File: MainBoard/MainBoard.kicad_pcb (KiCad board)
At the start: 2 copper layers, 111 parts, among them J1 DF40C-100DS-0.4V(51) _LFT, J2 DF40C-100DS-0.4V(51) _RFT (PN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, J3 HDMI_A, J4 Barrel_Jack, J7 USB_C_Receptacle, SW1 SW_Push, SW10 SW_Push, SW100 SW_Push, SW11 SW_Push, SW12 SW_Push, SW13 SW_Push, SW14 SW_Push, SW15 SW_Push, SW16 SW_Push, SW17 SW_Push, SW18 SW_Push, SW19 SW_Push, SW2 SW_Push, SW20 SW_Push, SW21 SW_Push, SW22 SW_Push, SW23 SW_Push, SW24 SW_Push, SW25 SW_Push, SW26 SW_Push, SW27 SW_Push, SW28 SW_Push, SW29 SW_Push, SW3 SW_Push, SW30 SW_Push, SW31 SW_Push, SW32 SW_Push, SW33 SW_Push, SW34 SW_Push, SW35 SW_Push, SW36 SW_Push, SW37 SW_Push, SW38 SW_Push, SW39 SW_Push, SW4 SW_Push, SW40 SW_Push, SW41 SW_Push, SW42 SW_Push, SW43 SW_Push, SW44 SW_Push, SW45 SW_Push, SW46 SW_Push, SW47 SW_Push, SW48 SW_Push, SW49 SW_Push, SW5 SW_Push, SW50 SW_Push, SW51 SW_Push, SW52 SW_Push, SW53 SW_Push, SW54 SW_Push, SW55 SW_Push, SW56 SW_Push, SW57 SW_Push, SW58 SW_Push, SW59 SW_Push, SW6 SW_Push, SW60 SW_Push, SW61 SW_Push, SW62 SW_Push, SW63 SW_Push, SW64 SW_Push, SW65 SW_Push, SW66 SW_Push, SW67 SW_Push, SW68 SW_Push, SW69 SW_Push, SW7 SW_Push, SW70 SW_Push, SW71 SW_Push, SW72 SW_Push, SW73 SW_Push, SW74 SW_Push, SW75 SW_Push, SW76 SW_Push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

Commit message: space out keyswitches for standard caps!
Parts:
- moved SW13 242.7 mm to (-15.0, 160.0)
- moved SW2 236.9 mm to (10.0, 160.0)
- moved SW5 231.4 mm to (35.0, 160.0)
- moved SW9 226.0 mm to (60.0, 160.0)
- moved SW1 217.0 mm to (-15.0, 140.0)
- moved SW14 215.3 mm to (95.0, 160.0)
- moved SW4 206.9 mm to (15.0, 140.0)
- moved SW20 203.5 mm to (135.0, 160.0)
- moved SW8 197.3 mm to (45.0, 140.0)
- moved SW27 195.7 mm to (170.0, 160.0)
- moved SW37 194.7 mm to (65.0, 140.0)
- moved SW3 194.6 mm to (-15.0, 120.0)
- moved SW35 192.6 mm to (195.0, 160.0)
- moved SW19 192.2 mm to (85.0, 140.0)
- moved SW43 191.4 mm to (215.0, 160.0)
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
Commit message: route keyboard
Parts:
- moved SW72 67.0 mm to (244.0, 138.0)
- moved SW1 66.5 mm to (49.0, 158.0)
- moved SW10 66.5 mm to (64.0, 98.0)
- moved SW100 66.5 mm to (304.0, 178.0)
- moved SW11 66.5 mm to (94.0, 118.0)
- moved SW13 66.5 mm to (49.0, 178.0)
- moved SW14 66.5 mm to (159.0, 178.0)
- moved SW15 66.5 mm to (64.0, 78.0)
- moved SW16 66.5 mm to (89.0, 98.0)
- moved SW17 66.5 mm to (114.0, 118.0)
- moved SW18 66.5 mm to (124.0, 138.0)
- moved SW19 66.5 mm to (149.0, 158.0)
- moved SW2 66.5 mm to (74.0, 178.0)
- moved SW20 66.5 mm to (199.0, 178.0)
- moved SW21 66.5 mm to (184.0, 78.1)
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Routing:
- net Net-(SW14-Pad1): track 0.00 -> 964.8 mm
- net Net-(SW13-Pad1): track 0.00 -> 893.0 mm
- net Net-(SW18-Pad1): track 0.00 -> 876.3 mm
- net Net-(SW12-Pad1): track 0.00 -> 848.7 mm
- net Net-(SW15-Pad1): track 0.00 -> 830.5 mm
- net Net-(SW19-Pad1): track 0.00 -> 780.6 mm
- net Net-(SW1-Pad1): track 0.00 -> 664.5 mm, vias 0 -> 2
- net Net-(SW17-Pad1): track 0.00 -> 630.5 mm
- net Net-(SW16-Pad1): track 0.00 -> 619.3 mm
- net Net-(SW10-Pad1): track 0.00 -> 573.6 mm
- net Net-(SW41-Pad2): track 0.00 -> 542.1 mm
- net Net-(SW21-Pad2): track 0.00 -> 525.9 mm
- net Net-(SW100-Pad2): track 0.00 -> 518.7 mm
- net Net-(SW51-Pad2): track 0.00 -> 494.6 mm
- net Net-(SW81-Pad2): track 0.00 -> 468.5 mm
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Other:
- board outline added: 340 x 200 mm
- copper layers 2 -> 6

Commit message: move power dilevery to a hierarchy sheet and wire HDMI1
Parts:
- moved J1 306.7 mm to (75.4, 239.0), turned to 180 degrees
- moved J2 267.2 mm to (75.4, 204.9), turned to 180 degrees
- moved U1 101.0 mm to (161.0, -53.0), turned to 270 degrees
- moved SW1 14.2 mm to (40.0, 147.0)
- moved SW10 14.2 mm to (55.0, 87.0)
- moved SW100 14.2 mm to (295.0, 167.0)
- moved SW11 14.2 mm to (85.0, 107.0)
- moved SW12 14.2 mm to (115.0, 67.0)
- moved SW13 14.2 mm to (40.0, 167.0)
- moved SW14 14.2 mm to (150.0, 167.0)
- moved SW15 14.2 mm to (55.0, 67.0)
- moved SW16 14.2 mm to (80.0, 87.0)
- moved SW17 14.2 mm to (105.0, 107.0)
- moved SW18 14.2 mm to (115.0, 127.0)
- moved SW19 14.2 mm to (140.0, 147.0)
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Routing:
- net Net-(SW31-Pad2): track 346.6 -> 380.4 mm
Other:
- board size 340 x 200 mm -> 340 x 230 mm

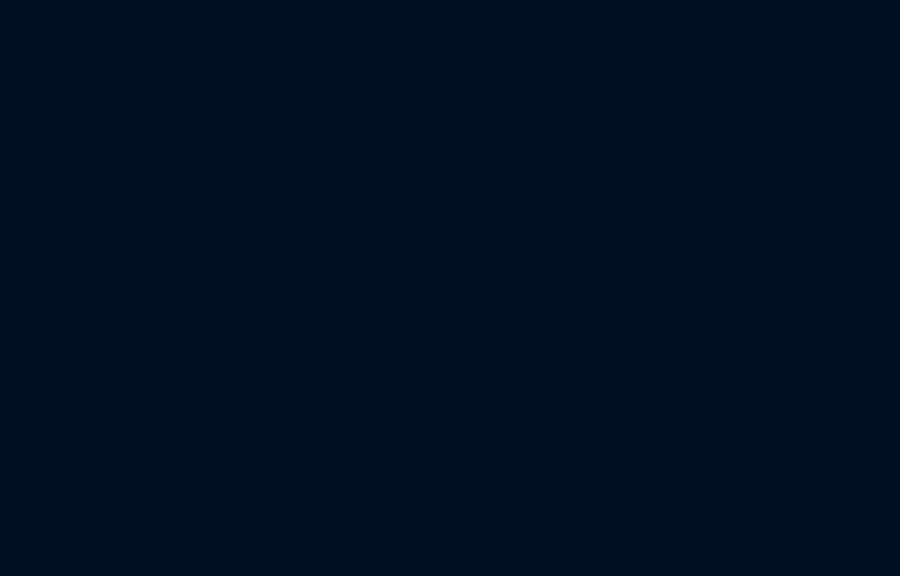
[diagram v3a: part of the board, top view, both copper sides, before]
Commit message: Add usb 3 chip in hierarchy sheet and wire ports
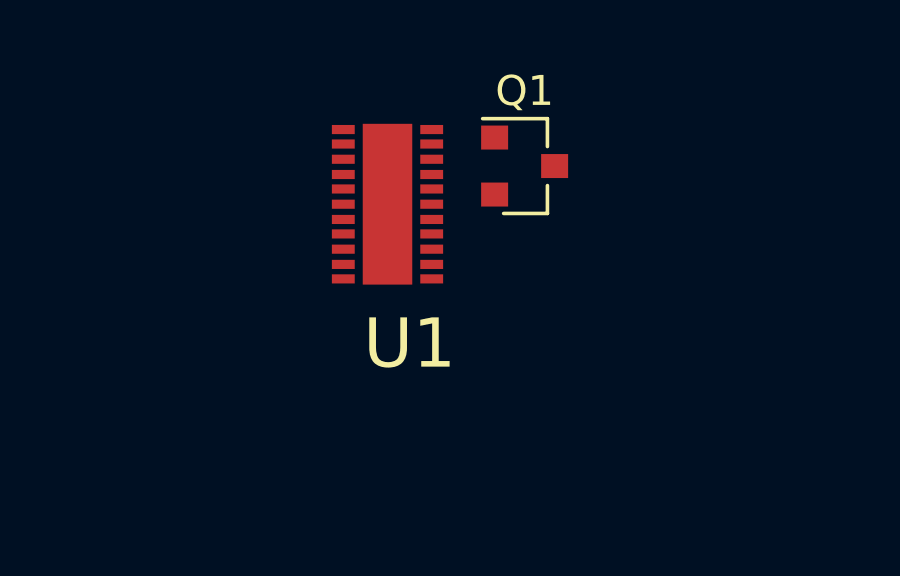
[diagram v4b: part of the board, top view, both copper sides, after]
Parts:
- added Q1: AO3401A, Package_TO_SOT_SMD:SOT-23, F.Cu at (185.5, -83.3)
- added U1: LTC4090EDJCPBF, Libs:DFN600X300X80-23N, F.Cu at (180.9, -82.0)
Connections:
- J3 pad 1: Net-(J3-Pad1) -> Net-(J2-Pad46)
- J3 pad 10: Net-(J3-Pad10) -> Net-(J2-Pad64)
- J3 pad 11: Net-(J3-Pad11) -> GND
- J3 pad 12: Net-(J3-Pad12) -> Net-(J2-Pad66)
- J3 pad 13: Net-(J3-Pad13) -> Net-(J2-Pad49)
- J3 pad 15: Net-(J3-Pad15) -> Net-(J2-Pad47)
- J3 pad 16: Net-(J3-Pad16) -> Net-(J2-Pad45)
- J3 pad 17: Net-(J3-Pad17) -> GND
- J3 pad 18: Net-(J3-Pad18) -> +5V
- J3 pad 19: Net-(J3-Pad19) -> Net-(J2-Pad43)
- J3 pad 2: Net-(J3-Pad2) -> GND
- J3 pad 3: Net-(J3-Pad3) -> Net-(J2-Pad48)
- J3 pad 4: Net-(J3-Pad4) -> Net-(J2-Pad52)
- J3 pad 5: Net-(J3-Pad5) -> GND
- J3 pad 6: Net-(J3-Pad6) -> Net-(J2-Pad54)
- J3 pad 7: Net-(J3-Pad7) -> Net-(J2-Pad58)
- J3 pad 8: Net-(J3-Pad8) -> GND
- J3 pad 9: Net-(J3-Pad9) -> Net-(J2-Pad60)
- J3 pad SH: Net-(J3-PadSH) -> GND
- J4 pad 2: Net-(J4-Pad2) -> /Power_Delivery/HV_IN
- J7 pad A4: Net-(J7-PadA4) -> /Power_Delivery/5v_IN
- J7 pad A5: Net-(J7-PadA5) -> Net-(J1-Pad96)
- J7 pad A9: Net-(J7-PadA4) -> /Power_Delivery/5v_IN
- J7 pad B4: Net-(J7-PadA4) -> /Power_Delivery/5v_IN
- J7 pad B5: Net-(J7-PadB5) -> Net-(J1-Pad94)
- J7 pad B9: Net-(J7-PadA4) -> /Power_Delivery/5v_IN

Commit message: mostly replace keyboard
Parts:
- removed BT2, BT3, BT4: _, Connector_JST:JST_PH_S2B-PH-SM4-TB_1x02-1MP_P2.00mm_Horizontal
- removed the U1 at (180.9, -82.0)
- removed the U1 at (161.0, -53.0)
- added C1: 270pF, LED_SMD:LED_0805_2012Metric_Castellated, F.Cu at (556.1, -145.0)
- added C2: 0.1uF, LED_SMD:LED_0805_2012Metric_Castellated, F.Cu at (565.8, -145.0)
- added C3: 4.7uF, LED_SMD:LED_0805_2012Metric_Castellated, F.Cu at (570.8, -154.1)
- added C4: 1uF, LED_SMD:LED_0805_2012Metric_Castellated, F.Cu at (561.0, -145.0)
- added C5: 0.47uF, LED_SMD:LED_0805_2012Metric_Castellated, F.Cu at (570.8, -157.0)
- added C6: 22uF, LED_SMD:LED_0805_2012Metric_Castellated, F.Cu at (556.1, -149.9)
- added D1: D_Schottky, LED_THT:LED_D1.8mm_W1.8mm_H2.4mm_Horizontal_O6.35mm_Z8.2mm, F.Cu at (564.1, -156.7)
- added J10: USB3_A, Connector_USB:USB3_A_Plug_Wuerth_692112030100_Horizontal, F.Cu at (479.2, -135.5)
- added J11: USB3_A (FAST), Connector_USB:USB3_A_Plug_Wuerth_692112030100_Horizontal, F.Cu at (479.2, -150.8)
- added J5: USB3_A, Connector_USB:USB3_A_Plug_Wuerth_692112030100_Horizontal, F.Cu at (525.6, -150.8)
- added J6: USB3_A, Connector_USB:USB3_A_Plug_Wuerth_692112030100_Horizontal, F.Cu at (502.4, -135.5)
- added J9: USB3_A, Connector_USB:USB3_A_Plug_Wuerth_692112030100_Horizontal, F.Cu at (502.4, -150.8)
- added U1: LTC4090EDJCPBF, Libs:DFN600X300X80-23N, F.Cu at (551.3, -147.8)
- added U3: CD74HC4067M, Package_SO:SOIC-24W_7.5x15.4mm_P1.27mm, F.Cu at (513.1, -111.5)
- added U4: TUSB8041, Package_DFN_QFN:QFN-64-1EP_9x9mm_P0.5mm_EP6x6mm_ThermalVias, F.Cu at (527.6, -137.5)
- BT1: value Battery Cell -> Battery_Cell; footprint Connector_JST:JST_PH_S2B-PH-SM4-TB_1x02-1MP_P2.00mm_Horizontal -> Connector_PinSocket_2.54mm:PinSocket_1x02_P2.54mm_Horizontal
- SW1, SW10, SW100, SW11, SW12, SW13, SW14, SW15, SW16, SW17, SW18, SW19, SW2, SW20, SW21, SW22, SW23, SW24, SW25, SW26, SW27, SW28, SW29, SW3, SW30, SW31, SW32, SW33, SW34, SW35, SW36, SW37, SW38, SW39, SW4, SW40, SW41, SW42, SW43, SW44, SW45, SW46, SW47, SW48, SW49, SW5, SW50, SW51, SW52, SW53, SW54, SW55, SW56, SW57, SW58, SW59, SW6, SW60, SW61, SW62, SW63, SW64, SW65, SW66, SW67, SW68, SW69, SW7, SW70, SW71, SW72, SW73, SW74, SW75, SW76, SW77, SW78, SW79, SW8, SW80, SW81, SW82, SW83, SW84, SW85, SW86, SW87, SW88, SW89, SW9, SW90, SW91, SW92, SW93, SW94, SW95, SW96, SW97, SW98, SW99: value SW_Push -> SW_MEC_5G; footprint Libs:SW_PG1350_reversible_rotatable -> Libs:Kailh_socket_PG1350
- moved J1 594.5 mm to (492.5, -184.6), turned to 0 degrees
- moved J2 566.9 mm to (492.5, -179.0), turned to 0 degrees
- moved U2 467.9 mm to (480.1, -115.6)
- moved Q1 390.9 mm to (570.6, -150.3)
- moved SW5 378.7 mm to (243.2, -179.3)
- moved SW94 345.7 mm to (50.0, 260.0)
- moved SW4 341.5 mm to (170.6, -179.3)
- moved SW11 336.3 mm to (261.4, -179.3)
- moved SW9 331.4 mm to (225.1, -145.6)
- moved BT1 322.6 mm to (560.1, -156.2)
- moved SW2 320.6 mm to (188.8, -128.8)
- moved SW3 319.7 mm to (206.9, -145.6)
- moved SW28 319.0 mm to (370.0, 180.0)
- moved SW95 314.5 mm to (75.0, 260.0)
- moved SW10 312.5 mm to (243.2, -162.5)
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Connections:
- net Net-(J2-Pad10) renamed PCIe_CLK_P
- net Net-(J2-Pad12) renamed PCIe_CLK_N
- net Net-(J2-Pad16) renamed PCIe_RX_P
- net Net-(J2-Pad18) renamed PCIe_RX_N
- net Net-(J2-Pad2) renamed PCIe_CLK_nREQ
- net Net-(J2-Pad22) renamed PCIe_TX_P
- net Net-(J2-Pad24) renamed PCIe_TX_N
- net Net-(J2-Pad9) renamed PCIe_nRST
- J7 pad A10: Net-(J7-PadA10) -> USBCRXN
- J7 pad A11: Net-(J7-PadA11) -> USBCRXP
- J7 pad A2: Net-(J7-PadA2) -> USBCTXP
- J7 pad A3: Net-(J7-PadA3) -> USBCTXN
- J7 pad A6: Net-(J7-PadA6) -> USBCP
- J7 pad A7: Net-(J7-PadA7) -> USBCM
- J7 pad B10: Net-(J7-PadB10) -> USBCRXN
- J7 pad B11: Net-(J7-PadB11) -> USBCRXP
- J7 pad B2: Net-(J7-PadB2) -> USBCTXP
- J7 pad B3: Net-(J7-PadB3) -> USBCTXN
- J7 pad B6: Net-(J7-PadB6) -> USBCP
- J7 pad B7: Net-(J7-PadB7) -> USBCM
- SW1 pad 2: Net-(SW1-Pad2) -> Net-(SW1-Pad1)
- SW10 pad 2: Net-(SW1-Pad2) -> Net-(SW10-Pad1)
- SW100 pad 1: Net-(SW10-Pad1) -> Net-(SW100-Pad1)
- SW100 pad 2: Net-(SW100-Pad2) -> Net-(SW100-Pad1)
- SW11 pad 1: Net-(SW1-Pad1) -> Net-(SW11-Pad1)
- SW11 pad 2: Net-(SW11-Pad2) -> Net-(SW11-Pad1)
- SW12 pad 2: Net-(SW11-Pad2) -> Net-(SW12-Pad1)
- SW13 pad 1: Net-(SW13-Pad1) -> Net-(SW1-Pad1)
- SW13 pad 2: Net-(SW11-Pad2) -> Net-(SW1-Pad1)
- SW14 pad 2: Net-(SW11-Pad2) -> Net-(SW14-Pad1)
- SW15 pad 2: Net-(SW11-Pad2) -> Net-(SW15-Pad1)
- SW16 pad 2: Net-(SW11-Pad2) -> Net-(SW16-Pad1)
- SW17 pad 2: Net-(SW11-Pad2) -> Net-(SW17-Pad1)
- SW18 pad 2: Net-(SW11-Pad2) -> Net-(SW18-Pad1)
- SW19 pad 1: Net-(SW19-Pad1) -> Net-(SW100-Pad1)
- SW19 pad 2: Net-(SW11-Pad2) -> Net-(SW100-Pad1)
- SW2 pad 1: Net-(SW12-Pad1) -> Net-(SW14-Pad1)
- SW2 pad 2: Net-(SW1-Pad2) -> Net-(SW14-Pad1)
- SW20 pad 1: Net-(SW10-Pad1) -> Net-(SW20-Pad1)
- SW20 pad 2: Net-(SW11-Pad2) -> Net-(SW20-Pad1)
- SW21 pad 1: Net-(SW1-Pad1) -> Net-(SW21-Pad1)
- SW21 pad 2: Net-(SW21-Pad2) -> Net-(SW21-Pad1)
- SW22 pad 1: Net-(SW12-Pad1) -> Net-(SW22-Pad1)
- SW22 pad 2: Net-(SW21-Pad2) -> Net-(SW22-Pad1)
- SW23 pad 1: Net-(SW13-Pad1) -> Net-(SW23-Pad1)
- SW23 pad 2: Net-(SW21-Pad2) -> Net-(SW23-Pad1)
- SW24 pad 1: Net-(SW14-Pad1) -> Net-(SW10-Pad1)
- SW24 pad 2: Net-(SW21-Pad2) -> Net-(SW10-Pad1)
- SW25 pad 1: Net-(SW15-Pad1) -> Net-(SW25-Pad1)
- SW25 pad 2: Net-(SW21-Pad2) -> Net-(SW25-Pad1)
- SW26 pad 1: Net-(SW16-Pad1) -> Net-(SW11-Pad1)
- SW26 pad 2: Net-(SW21-Pad2) -> Net-(SW11-Pad1)
- SW27 pad 1: Net-(SW17-Pad1) -> Net-(SW27-Pad1)
- SW27 pad 2: Net-(SW21-Pad2) -> Net-(SW27-Pad1)
- SW28 pad 1: Net-(SW18-Pad1) -> Net-(SW27-Pad1)
- SW28 pad 2: Net-(SW21-Pad2) -> Net-(SW27-Pad1)
- SW29 pad 1: Net-(SW19-Pad1) -> Net-(SW12-Pad1)
- SW29 pad 2: Net-(SW21-Pad2) -> Net-(SW12-Pad1)
- SW3 pad 1: Net-(SW13-Pad1) -> Net-(SW15-Pad1)
- SW3 pad 2: Net-(SW1-Pad2) -> Net-(SW15-Pad1)
- SW30 pad 1: Net-(SW10-Pad1) -> Net-(SW1-Pad1)
- SW30 pad 2: Net-(SW21-Pad2) -> Net-(SW1-Pad1)
- SW31 pad 1: Net-(SW1-Pad1) -> Net-(SW15-Pad1)
- SW31 pad 2: Net-(SW31-Pad2) -> Net-(SW15-Pad1)
- SW32 pad 1: Net-(SW12-Pad1) -> Net-(SW16-Pad1)
- SW32 pad 2: Net-(SW31-Pad2) -> Net-(SW16-Pad1)
- SW33 pad 1: Net-(SW13-Pad1) -> Net-(SW17-Pad1)
- SW33 pad 2: Net-(SW31-Pad2) -> Net-(SW17-Pad1)
- SW34 pad 1: Net-(SW14-Pad1) -> Net-(SW18-Pad1)
- SW34 pad 2: Net-(SW31-Pad2) -> Net-(SW18-Pad1)
- SW35 pad 1: Net-(SW15-Pad1) -> Net-(SW100-Pad1)
- SW35 pad 2: Net-(SW31-Pad2) -> Net-(SW100-Pad1)
- SW36 pad 1: Net-(SW16-Pad1) -> Net-(SW20-Pad1)
- SW36 pad 2: Net-(SW31-Pad2) -> Net-(SW20-Pad1)
- SW37 pad 1: Net-(SW17-Pad1) -> Net-(SW21-Pad1)
- SW37 pad 2: Net-(SW31-Pad2) -> Net-(SW21-Pad1)
- SW38 pad 1: Net-(SW18-Pad1) -> Net-(SW22-Pad1)
- SW38 pad 2: Net-(SW31-Pad2) -> Net-(SW22-Pad1)
- SW39 pad 1: Net-(SW19-Pad1) -> Net-(SW23-Pad1)
- SW39 pad 2: Net-(SW31-Pad2) -> Net-(SW23-Pad1)
- SW4 pad 1: Net-(SW14-Pad1) -> Net-(SW16-Pad1)
- SW4 pad 2: Net-(SW1-Pad2) -> Net-(SW16-Pad1)
- SW40 pad 2: Net-(SW31-Pad2) -> Net-(SW10-Pad1)
- SW41 pad 1: Net-(SW1-Pad1) -> Net-(SW25-Pad1)
- SW41 pad 2: Net-(SW41-Pad2) -> Net-(SW25-Pad1)
- SW42 pad 1: Net-(SW12-Pad1) -> Net-(SW11-Pad1)
- SW42 pad 2: Net-(SW41-Pad2) -> Net-(SW11-Pad1)
- SW43 pad 1: Net-(SW13-Pad1) -> Net-(SW12-Pad1)
- SW43 pad 2: Net-(SW41-Pad2) -> Net-(SW12-Pad1)
- SW44 pad 2: Net-(SW41-Pad2) -> Net-(SW14-Pad1)
- SW45 pad 2: Net-(SW41-Pad2) -> Net-(SW15-Pad1)
- SW46 pad 2: Net-(SW41-Pad2) -> Net-(SW16-Pad1)
- SW47 pad 2: Net-(SW41-Pad2) -> Net-(SW17-Pad1)
- SW48 pad 2: Net-(SW41-Pad2) -> Net-(SW18-Pad1)
- SW49 pad 1: Net-(SW19-Pad1) -> Net-(SW100-Pad1)
- SW49 pad 2: Net-(SW41-Pad2) -> Net-(SW100-Pad1)
- SW5 pad 1: Net-(SW15-Pad1) -> Net-(SW17-Pad1)
- SW5 pad 2: Net-(SW1-Pad2) -> Net-(SW17-Pad1)
- SW50 pad 1: Net-(SW10-Pad1) -> Net-(SW20-Pad1)
- SW50 pad 2: Net-(SW41-Pad2) -> Net-(SW20-Pad1)
- SW51 pad 1: Net-(SW1-Pad1) -> Net-(SW21-Pad1)
- SW51 pad 2: Net-(SW51-Pad2) -> Net-(SW21-Pad1)
- SW52 pad 1: Net-(SW12-Pad1) -> Net-(SW22-Pad1)
- SW52 pad 2: Net-(SW51-Pad2) -> Net-(SW22-Pad1)
- SW53 pad 1: Net-(SW13-Pad1) -> Net-(SW23-Pad1)
- SW53 pad 2: Net-(SW51-Pad2) -> Net-(SW23-Pad1)
- SW54 pad 1: Net-(SW14-Pad1) -> Net-(SW10-Pad1)
- SW54 pad 2: Net-(SW51-Pad2) -> Net-(SW10-Pad1)
- SW55 pad 1: Net-(SW15-Pad1) -> Net-(SW25-Pad1)
- SW55 pad 2: Net-(SW51-Pad2) -> Net-(SW25-Pad1)
- SW56 pad 1: Net-(SW16-Pad1) -> Net-(SW11-Pad1)
- SW56 pad 2: Net-(SW51-Pad2) -> Net-(SW11-Pad1)
- SW57 pad 1: Net-(SW17-Pad1) -> Net-(SW27-Pad1)
- SW57 pad 2: Net-(SW51-Pad2) -> Net-(SW27-Pad1)
- SW58 pad 1: Net-(SW18-Pad1) -> Net-(SW12-Pad1)
- SW58 pad 2: Net-(SW51-Pad2) -> Net-(SW12-Pad1)
- SW59 pad 1: Net-(SW19-Pad1) -> Net-(SW1-Pad1)
- SW59 pad 2: Net-(SW51-Pad2) -> Net-(SW1-Pad1)
- SW6 pad 1: Net-(SW16-Pad1) -> Net-(SW100-Pad1)
- SW6 pad 2: Net-(SW1-Pad2) -> Net-(SW100-Pad1)
- SW60 pad 1: Net-(SW10-Pad1) -> Net-(SW14-Pad1)
- SW60 pad 2: Net-(SW51-Pad2) -> Net-(SW14-Pad1)
- SW61 pad 1: Net-(SW1-Pad1) -> Net-(SW15-Pad1)
- SW61 pad 2: Net-(SW61-Pad2) -> Net-(SW15-Pad1)
- SW62 pad 1: Net-(SW12-Pad1) -> Net-(SW16-Pad1)
- SW62 pad 2: Net-(SW61-Pad2) -> Net-(SW16-Pad1)
- SW63 pad 1: Net-(SW13-Pad1) -> Net-(SW17-Pad1)
- SW63 pad 2: Net-(SW61-Pad2) -> Net-(SW17-Pad1)
- SW64 pad 1: Net-(SW14-Pad1) -> Net-(SW18-Pad1)
- SW64 pad 2: Net-(SW61-Pad2) -> Net-(SW18-Pad1)
- SW65 pad 1: Net-(SW15-Pad1) -> Net-(SW100-Pad1)
- SW65 pad 2: Net-(SW61-Pad2) -> Net-(SW100-Pad1)
- SW66 pad 1: Net-(SW16-Pad1) -> Net-(SW20-Pad1)
- SW66 pad 2: Net-(SW61-Pad2) -> Net-(SW20-Pad1)
- SW67 pad 1: Net-(SW17-Pad1) -> Net-(SW21-Pad1)
- SW67 pad 2: Net-(SW61-Pad2) -> Net-(SW21-Pad1)
- SW68 pad 1: Net-(SW18-Pad1) -> Net-(SW22-Pad1)
- SW68 pad 2: Net-(SW61-Pad2) -> Net-(SW22-Pad1)
- SW69 pad 1: Net-(SW19-Pad1) -> Net-(SW23-Pad1)
- SW69 pad 2: Net-(SW61-Pad2) -> Net-(SW23-Pad1)
- SW7 pad 1: Net-(SW17-Pad1) -> Net-(SW20-Pad1)
- SW7 pad 2: Net-(SW1-Pad2) -> Net-(SW20-Pad1)
- SW70 pad 2: Net-(SW61-Pad2) -> Net-(SW10-Pad1)
- SW71 pad 1: Net-(SW1-Pad1) -> Net-(SW11-Pad1)
- SW71 pad 2: Net-(SW71-Pad2) -> Net-(SW11-Pad1)
- SW72 pad 1: Net-(SW12-Pad1) -> Net-(SW27-Pad1)
- SW72 pad 2: Net-(SW71-Pad2) -> Net-(SW27-Pad1)
- SW73 pad 1: Net-(SW13-Pad1) -> Net-(SW12-Pad1)
- SW73 pad 2: Net-(SW71-Pad2) -> Net-(SW12-Pad1)
- SW74 pad 1: Net-(SW14-Pad1) -> Net-(SW1-Pad1)
- SW74 pad 2: Net-(SW71-Pad2) -> Net-(SW1-Pad1)
- SW75 pad 1: Net-(SW15-Pad1) -> Net-(SW14-Pad1)
- SW75 pad 2: Net-(SW71-Pad2) -> Net-(SW14-Pad1)
- SW76 pad 1: Net-(SW16-Pad1) -> Net-(SW15-Pad1)
- SW76 pad 2: Net-(SW71-Pad2) -> Net-(SW15-Pad1)
- SW77 pad 1: Net-(SW17-Pad1) -> Net-(SW16-Pad1)
- SW77 pad 2: Net-(SW71-Pad2) -> Net-(SW16-Pad1)
- SW78 pad 1: Net-(SW18-Pad1) -> Net-(SW17-Pad1)
- SW78 pad 2: Net-(SW71-Pad2) -> Net-(SW17-Pad1)
- SW79 pad 1: Net-(SW19-Pad1) -> Net-(SW18-Pad1)
- SW79 pad 2: Net-(SW71-Pad2) -> Net-(SW18-Pad1)
- SW8 pad 1: Net-(SW18-Pad1) -> Net-(SW21-Pad1)
- SW8 pad 2: Net-(SW1-Pad2) -> Net-(SW21-Pad1)
- SW80 pad 1: Net-(SW10-Pad1) -> Net-(SW100-Pad1)
- SW80 pad 2: Net-(SW71-Pad2) -> Net-(SW100-Pad1)
- SW81 pad 1: Net-(SW1-Pad1) -> Net-(SW20-Pad1)
- SW81 pad 2: Net-(SW81-Pad2) -> Net-(SW20-Pad1)
- SW82 pad 1: Net-(SW12-Pad1) -> Net-(SW21-Pad1)
- SW82 pad 2: Net-(SW81-Pad2) -> Net-(SW21-Pad1)
- SW83 pad 1: Net-(SW13-Pad1) -> Net-(SW22-Pad1)
- SW83 pad 2: Net-(SW81-Pad2) -> Net-(SW22-Pad1)
- SW84 pad 1: Net-(SW14-Pad1) -> Net-(SW23-Pad1)
- SW84 pad 2: Net-(SW81-Pad2) -> Net-(SW23-Pad1)
- SW85 pad 1: Net-(SW15-Pad1) -> Net-(SW11-Pad1)
- SW85 pad 2: Net-(SW81-Pad2) -> Net-(SW11-Pad1)
- SW86 pad 1: Net-(SW16-Pad1) -> Net-(SW27-Pad1)
- SW86 pad 2: Net-(SW81-Pad2) -> Net-(SW27-Pad1)
- SW87 pad 1: Net-(SW17-Pad1) -> Net-(SW10-Pad1)
- SW87 pad 2: Net-(SW81-Pad2) -> Net-(SW10-Pad1)
- SW88 pad 1: Net-(SW18-Pad1) -> Net-(SW20-Pad1)
- SW88 pad 2: Net-(SW81-Pad2) -> Net-(SW20-Pad1)
- SW89 pad 1: Net-(SW19-Pad1) -> Net-(SW22-Pad1)
- SW89 pad 2: Net-(SW81-Pad2) -> Net-(SW22-Pad1)
- SW9 pad 1: Net-(SW19-Pad1) -> Net-(SW23-Pad1)
- SW9 pad 2: Net-(SW1-Pad2) -> Net-(SW23-Pad1)
- SW90 pad 1: Net-(SW10-Pad1) -> Net-(SW23-Pad1)
- SW90 pad 2: Net-(SW81-Pad2) -> Net-(SW23-Pad1)
- SW91 pad 1: Net-(SW1-Pad1) -> Net-(SW10-Pad1)
- SW91 pad 2: Net-(SW100-Pad2) -> Net-(SW10-Pad1)
- SW92 pad 1: Net-(SW12-Pad1) -> Net-(SW11-Pad1)
- SW92 pad 2: Net-(SW100-Pad2) -> Net-(SW11-Pad1)
- SW93 pad 1: Net-(SW13-Pad1) -> Net-(SW27-Pad1)
- SW93 pad 2: Net-(SW100-Pad2) -> Net-(SW27-Pad1)
- SW94 pad 1: Net-(SW14-Pad1) -> Net-(SW12-Pad1)
- SW94 pad 2: Net-(SW100-Pad2) -> Net-(SW12-Pad1)
- SW95 pad 1: Net-(SW15-Pad1) -> Net-(SW1-Pad1)
- SW95 pad 2: Net-(SW100-Pad2) -> Net-(SW1-Pad1)
- SW96 pad 1: Net-(SW16-Pad1) -> Net-(SW14-Pad1)
- SW96 pad 2: Net-(SW100-Pad2) -> Net-(SW14-Pad1)
- SW97 pad 1: Net-(SW17-Pad1) -> Net-(SW15-Pad1)
- SW97 pad 2: Net-(SW100-Pad2) -> Net-(SW15-Pad1)
- SW98 pad 1: Net-(SW18-Pad1) -> Net-(SW16-Pad1)
- SW98 pad 2: Net-(SW100-Pad2) -> Net-(SW16-Pad1)
- SW99 pad 1: Net-(SW19-Pad1) -> Net-(SW17-Pad1)
- SW99 pad 2: Net-(SW100-Pad2) -> Net-(SW17-Pad1)
- U2 pad 1: Net-(SW51-Pad2) -> Net-(U2-Pad1)
- U2 pad 12: Net-(SW11-Pad2) -> Net-(SW28-Pad3)
- U2 pad 19: Net-(SW100-Pad2) -> Net-(U2-Pad19)
- U2 pad 20: Net-(SW19-Pad1) -> Net-(U2-Pad20)
- U2 pad 21: Net-(SW18-Pad1) -> Net-(U2-Pad21)
- U2 pad 25: Net-(SW81-Pad2) -> Net-(U2-Pad25)
- U2 pad 26: Net-(SW1-Pad2) -> Net-(SW43-Pad3)
- U2 pad 27: Net-(SW61-Pad2) -> Net-(U2-Pad27)
- U2 pad 28: Net-(SW41-Pad2) -> Net-(U2-Pad28)
- U2 pad 29: Net-(SW31-Pad2) -> Net-(SW1-Pad3)
- U2 pad 30: Net-(SW21-Pad2) -> Net-(SW12-Pad3)
- U2 pad 31: Net-(SW71-Pad2) -> Net-(U2-Pad31)
- U2 pad 32: Net-(SW1-Pad1) -> Net-(SW58-Pad3)
- U2 pad 36: Net-(SW12-Pad1) -> Net-(SW73-Pad3)
- U2 pad 37: Net-(SW13-Pad1) -> Net-(SW100-Pad3)
- U2 pad 38: Net-(SW14-Pad1) -> Net-(U2-Pad38)
- U2 pad 39: Net-(SW15-Pad1) -> Net-(U2-Pad39)
- U2 pad 40: Net-(SW16-Pad1) -> Net-(U2-Pad40)
- U2 pad 41: Net-(SW17-Pad1) -> Net-(U2-Pad41)
- U2 pad 9: Net-(SW10-Pad1) -> Net-(U2-Pad9)
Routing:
- net Net-(SW14-Pad1): track 964.8 -> 0.00 mm
- net Net-(SW13-Pad1): track 893.0 -> 0.00 mm
- net Net-(SW18-Pad1): track 876.3 -> 0.00 mm
- net Net-(SW12-Pad1): track 848.7 -> 0.00 mm
- net Net-(SW15-Pad1): track 830.5 -> 0.00 mm
- net Net-(SW19-Pad1): track 780.6 -> 0.00 mm
- net Net-(SW1-Pad1): track 664.5 -> 0.00 mm, vias 2 -> 0
- net Net-(SW17-Pad1): track 630.5 -> 0.00 mm
- net Net-(SW16-Pad1): track 619.3 -> 0.00 mm
- net Net-(SW10-Pad1): track 573.6 -> 0.00 mm
- net Net-(SW41-Pad2): track 542.1 -> 0.00 mm
- net Net-(SW21-Pad2): track 525.9 -> 0.00 mm
- net Net-(SW100-Pad2): track 518.7 -> 0.00 mm
- net Net-(SW51-Pad2): track 494.6 -> 0.00 mm
- net Net-(SW81-Pad2): track 468.5 -> 0.00 mm
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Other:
- board outline removed

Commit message: mostly replace keyboard
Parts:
- moved U3 373.7 mm to (205.0, 100.0), turned to 180 degrees
- moved U2 301.5 mm to (255.0, 85.0), turned to 270 degrees

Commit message: finish keyboard, do some USB/PCIe routing
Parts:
- added U5: UPD720201K8-711-BAC-A, Libs:UPD720201K8-711-BAC-A, F.Cu at (219.8, 294.3)
- added U6: MX25L5121EMC-20G, Libs:MX25L5121EMC-20G, F.Cu at (236.0, 295.0)
- U2, U3: moved to B.Cu
- moved J5 657.4 mm to (51.0, 304.0), turned to 180 degrees
- moved J9 625.4 mm to (51.0, 282.0), turned to 180 degrees
- moved J2 556.0 mm to (226.0, 309.0)
- moved J10 555.8 mm to (139.5, 304.5), turned to 270 degrees
- moved U4 544.0 mm to (181.1, 281.9), turned to 270 degrees
- moved J1 531.3 mm to (226.0, 275.0)
- moved J3 488.1 mm to (373.2, 282.5), turned to 90 degrees
- moved J11 463.2 mm to (368.8, 299.0)
- moved J6 452.1 mm to (358.3, 293.1), turned to 180 degrees
- moved BT1 403.1 mm to (357.0, 192.0)
- moved C2 395.8 mm to (345.8, 184.0)
- moved C3 395.8 mm to (350.8, 174.9)
- moved C5 395.8 mm to (350.8, 172.0)
- moved C1 395.8 mm to (336.1, 184.0)
- moved C4 395.8 mm to (341.0, 184.0)
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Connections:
- SW1 pad 3: (no net) -> Net-(SW1-Pad3)
- SW10 pad 3: (no net) -> Net-(SW1-Pad3)
- SW100 pad 3: (no net) -> Net-(SW100-Pad3)
- SW11 pad 3: (no net) -> Net-(SW1-Pad3)
- SW12 pad 3: (no net) -> Net-(SW12-Pad3)
- SW13 pad 3: (no net) -> Net-(SW12-Pad3)
- SW14 pad 3: (no net) -> Net-(SW12-Pad3)
- SW15 pad 3: (no net) -> Net-(SW12-Pad3)
- SW16 pad 3: (no net) -> Net-(SW12-Pad3)
- SW17 pad 3: (no net) -> Net-(SW12-Pad3)
- SW18 pad 3: (no net) -> Net-(SW12-Pad3)
- SW19 pad 3: (no net) -> Net-(SW12-Pad3)
- SW2 pad 3: (no net) -> Net-(SW1-Pad3)
- SW20 pad 3: (no net) -> Net-(SW12-Pad3)
- SW21 pad 3: (no net) -> Net-(SW12-Pad3)
- SW22 pad 3: (no net) -> Net-(SW12-Pad3)
- SW23 pad 3: (no net) -> Net-(SW12-Pad3)
- SW24 pad 3: (no net) -> Net-(SW12-Pad3)
- SW25 pad 3: (no net) -> Net-(SW12-Pad3)
- SW26 pad 3: (no net) -> Net-(SW12-Pad3)
- SW27 pad 3: (no net) -> Net-(SW12-Pad3)
- SW28 pad 3: (no net) -> Net-(SW28-Pad3)
- SW29 pad 3: (no net) -> Net-(SW28-Pad3)
- SW3 pad 3: (no net) -> Net-(SW1-Pad3)
- SW30 pad 3: (no net) -> Net-(SW28-Pad3)
- SW31 pad 3: (no net) -> Net-(SW28-Pad3)
- SW32 pad 3: (no net) -> Net-(SW28-Pad3)
- SW33 pad 3: (no net) -> Net-(SW28-Pad3)
- SW34 pad 3: (no net) -> Net-(SW28-Pad3)
- SW35 pad 3: (no net) -> Net-(SW28-Pad3)
- SW36 pad 3: (no net) -> Net-(SW28-Pad3)
- SW37 pad 3: (no net) -> Net-(SW28-Pad3)
- SW38 pad 3: (no net) -> Net-(SW28-Pad3)
- SW39 pad 3: (no net) -> Net-(SW28-Pad3)
- SW4 pad 3: (no net) -> Net-(SW1-Pad3)
- SW40 pad 3: (no net) -> Net-(SW28-Pad3)
- SW41 pad 3: (no net) -> Net-(SW28-Pad3)
- SW42 pad 3: (no net) -> Net-(SW28-Pad3)
- SW43 pad 3: (no net) -> Net-(SW43-Pad3)
- SW44 pad 3: (no net) -> Net-(SW43-Pad3)
- SW45 pad 3: (no net) -> Net-(SW43-Pad3)
- SW46 pad 3: (no net) -> Net-(SW43-Pad3)
- SW47 pad 3: (no net) -> Net-(SW43-Pad3)
- SW48 pad 3: (no net) -> Net-(SW43-Pad3)
- SW49 pad 3: (no net) -> Net-(SW43-Pad3)
- SW5 pad 3: (no net) -> Net-(SW1-Pad3)
- SW50 pad 3: (no net) -> Net-(SW43-Pad3)
- SW51 pad 3: (no net) -> Net-(SW43-Pad3)
- SW52 pad 3: (no net) -> Net-(SW43-Pad3)
- SW53 pad 3: (no net) -> Net-(SW43-Pad3)
- SW54 pad 3: (no net) -> Net-(SW43-Pad3)
- SW55 pad 3: (no net) -> Net-(SW43-Pad3)
- SW56 pad 3: (no net) -> Net-(SW43-Pad3)
- SW57 pad 3: (no net) -> Net-(SW43-Pad3)
- SW58 pad 3: (no net) -> Net-(SW58-Pad3)
- SW59 pad 3: (no net) -> Net-(SW58-Pad3)
- SW6 pad 3: (no net) -> Net-(SW1-Pad3)
- SW60 pad 3: (no net) -> Net-(SW58-Pad3)
- SW61 pad 3: (no net) -> Net-(SW58-Pad3)
- SW62 pad 3: (no net) -> Net-(SW58-Pad3)
- SW63 pad 3: (no net) -> Net-(SW58-Pad3)
- SW64 pad 3: (no net) -> Net-(SW58-Pad3)
- SW65 pad 3: (no net) -> Net-(SW58-Pad3)
- SW66 pad 3: (no net) -> Net-(SW58-Pad3)
- SW67 pad 3: (no net) -> Net-(SW58-Pad3)
- SW68 pad 3: (no net) -> Net-(SW58-Pad3)
- SW69 pad 3: (no net) -> Net-(SW58-Pad3)
- SW7 pad 3: (no net) -> Net-(SW1-Pad3)
- SW70 pad 3: (no net) -> Net-(SW58-Pad3)
- SW71 pad 3: (no net) -> Net-(SW58-Pad3)
- SW72 pad 3: (no net) -> Net-(SW58-Pad3)
- SW73 pad 3: (no net) -> Net-(SW73-Pad3)
- SW74 pad 3: (no net) -> Net-(SW73-Pad3)
- SW75 pad 3: (no net) -> Net-(SW73-Pad3)
- SW76 pad 3: (no net) -> Net-(SW73-Pad3)
- SW77 pad 3: (no net) -> Net-(SW73-Pad3)
- SW78 pad 3: (no net) -> Net-(SW73-Pad3)
- SW79 pad 3: (no net) -> Net-(SW73-Pad3)
- SW8 pad 3: (no net) -> Net-(SW1-Pad3)
- SW80 pad 3: (no net) -> Net-(SW73-Pad3)
- SW81 pad 3: (no net) -> Net-(SW73-Pad3)
- SW82 pad 3: (no net) -> Net-(SW73-Pad3)
- SW83 pad 3: (no net) -> Net-(SW73-Pad3)
- SW84 pad 3: (no net) -> Net-(SW73-Pad3)
- SW85 pad 3: (no net) -> Net-(SW73-Pad3)
- SW86 pad 3: (no net) -> Net-(SW73-Pad3)
- SW87 pad 3: (no net) -> Net-(SW73-Pad3)
- SW88 pad 3: (no net) -> Net-(SW100-Pad3)
- SW89 pad 3: (no net) -> Net-(SW100-Pad3)
- SW9 pad 3: (no net) -> Net-(SW1-Pad3)
- SW90 pad 3: (no net) -> Net-(SW100-Pad3)
- SW91 pad 3: (no net) -> Net-(SW100-Pad3)
- SW92 pad 3: (no net) -> Net-(SW100-Pad3)
- SW93 pad 3: (no net) -> Net-(SW100-Pad3)
- SW94 pad 3: (no net) -> Net-(SW100-Pad3)
- SW95 pad 3: (no net) -> Net-(SW100-Pad3)
- SW96 pad 3: (no net) -> Net-(SW100-Pad3)
- SW97 pad 3: (no net) -> Net-(SW100-Pad3)
- SW98 pad 3: (no net) -> Net-(SW100-Pad3)
- SW99 pad 3: (no net) -> Net-(SW100-Pad3)
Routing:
- net Net-(SW12-Pad1): track 0.00 -> 443.9 mm, vias 0 -> 2
- net Net-(SW1-Pad1): track 0.00 -> 432.9 mm, vias 0 -> 2
- net Net-(U2-Pad31): track 0.00 -> 424.9 mm, vias 0 -> 2
- net Net-(SW14-Pad1): track 0.00 -> 411.1 mm, vias 0 -> 2
- net Net-(SW100-Pad3): track 0.00 -> 410.7 mm
- net Net-(U2-Pad1): track 0.00 -> 402.1 mm, vias 0 -> 2
- net Net-(SW15-Pad1): track 0.00 -> 395.7 mm, vias 0 -> 2
- net Net-(U2-Pad19): track 0.00 -> 394.4 mm, vias 0 -> 2
- net Net-(SW73-Pad3): track 0.00 -> 390.9 mm, vias 0 -> 2
- net Net-(U2-Pad25): track 0.00 -> 383.9 mm, vias 0 -> 3
- net Net-(SW16-Pad1): track 0.00 -> 378.0 mm, vias 0 -> 2
- net Net-(U2-Pad28): track 0.00 -> 374.9 mm, vias 0 -> 2
- net Net-(U2-Pad27): track 0.00 -> 374.5 mm, vias 0 -> 2
- net Net-(SW17-Pad1): track 0.00 -> 373.1 mm, vias 0 -> 2
- net Net-(SW58-Pad3): track 0.00 -> 372.2 mm
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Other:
- board outline added: 350 x 195 mm
- copper layers 6 -> 4
- net class Default: clearance 0.2 -> 0.1
- rule trace_clearance: 0.2 -> 0.1

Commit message: remove USB ss HUB IC and add onboard USB SATA bridge
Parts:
- removed J1: DF40C-100DS-0.4V(51) _LFT, Libs:HRS_DF40C-100DS-0.4V(51)
- removed J10, J5, J6, J9: USB3_A, Connector_USB:USB3_A_Plug_Wuerth_692112030100_Horizontal
- removed J11: USB3_A (FAST), Connector_USB:USB3_A_Plug_Wuerth_692112030100_Horizontal
- removed J2: DF40C-100DS-0.4V(51) _RFT (PN + 100), Libs:HRS_DF40C-100DS-0.4V(51)
- removed J3: HDMI_A, Connector_HDMI:HDMI_A_Contact_Technology_HDMI-19APL2_Horizontal
- removed J7: USB_C_Receptacle, Connector_USB:USB_C_Receptacle_Amphenol_12401548E4-2A
- removed U4: TUSB8041, Package_DFN_QFN:QFN-64-1EP_9x9mm_P0.5mm_EP6x6mm_ThermalVias
- removed U5: UPD720201K8-711-BAC-A, Libs:UPD720201K8-711-BAC-A
- removed U6: MX25L5121EMC-20G, Libs:MX25L5121EMC-20G
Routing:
- net Net-(J5-Pad9): track 187.8 -> 0.00 mm, vias 2 -> 0
- net Net-(J5-Pad8): track 182.0 -> 0.00 mm, vias 2 -> 0
- net Net-(J5-Pad2): track 181.7 -> 0.00 mm, vias 2 -> 0
- net Net-(J5-Pad3): track 177.8 -> 0.00 mm
- net Net-(J5-Pad6): track 173.7 -> 0.00 mm
- net Net-(J5-Pad5): track 170.0 -> 0.00 mm
- net Net-(J9-Pad3): track 138.5 -> 0.00 mm
- net Net-(J9-Pad9): track 134.1 -> 0.00 mm, vias 2 -> 0
- net Net-(J9-Pad6): track 129.6 -> 0.00 mm
- net Net-(J9-Pad2): track 127.4 -> 0.00 mm, vias 2 -> 0
- net Net-(J9-Pad8): track 126.8 -> 0.00 mm, vias 2 -> 0
- net Net-(J9-Pad5): track 125.2 -> 0.00 mm
- net /keyboard/USB_D+: track 268.4 -> 204.0 mm, vias 1 -> 0
- net /keyboard/USB_D-: track 267.0 -> 203.7 mm, vias 1 -> 0
- net Net-(U4-Pad59): track 39.6 -> 0.00 mm, vias 2 -> 0
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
